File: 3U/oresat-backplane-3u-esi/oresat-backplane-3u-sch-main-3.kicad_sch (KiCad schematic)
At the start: 28 parts

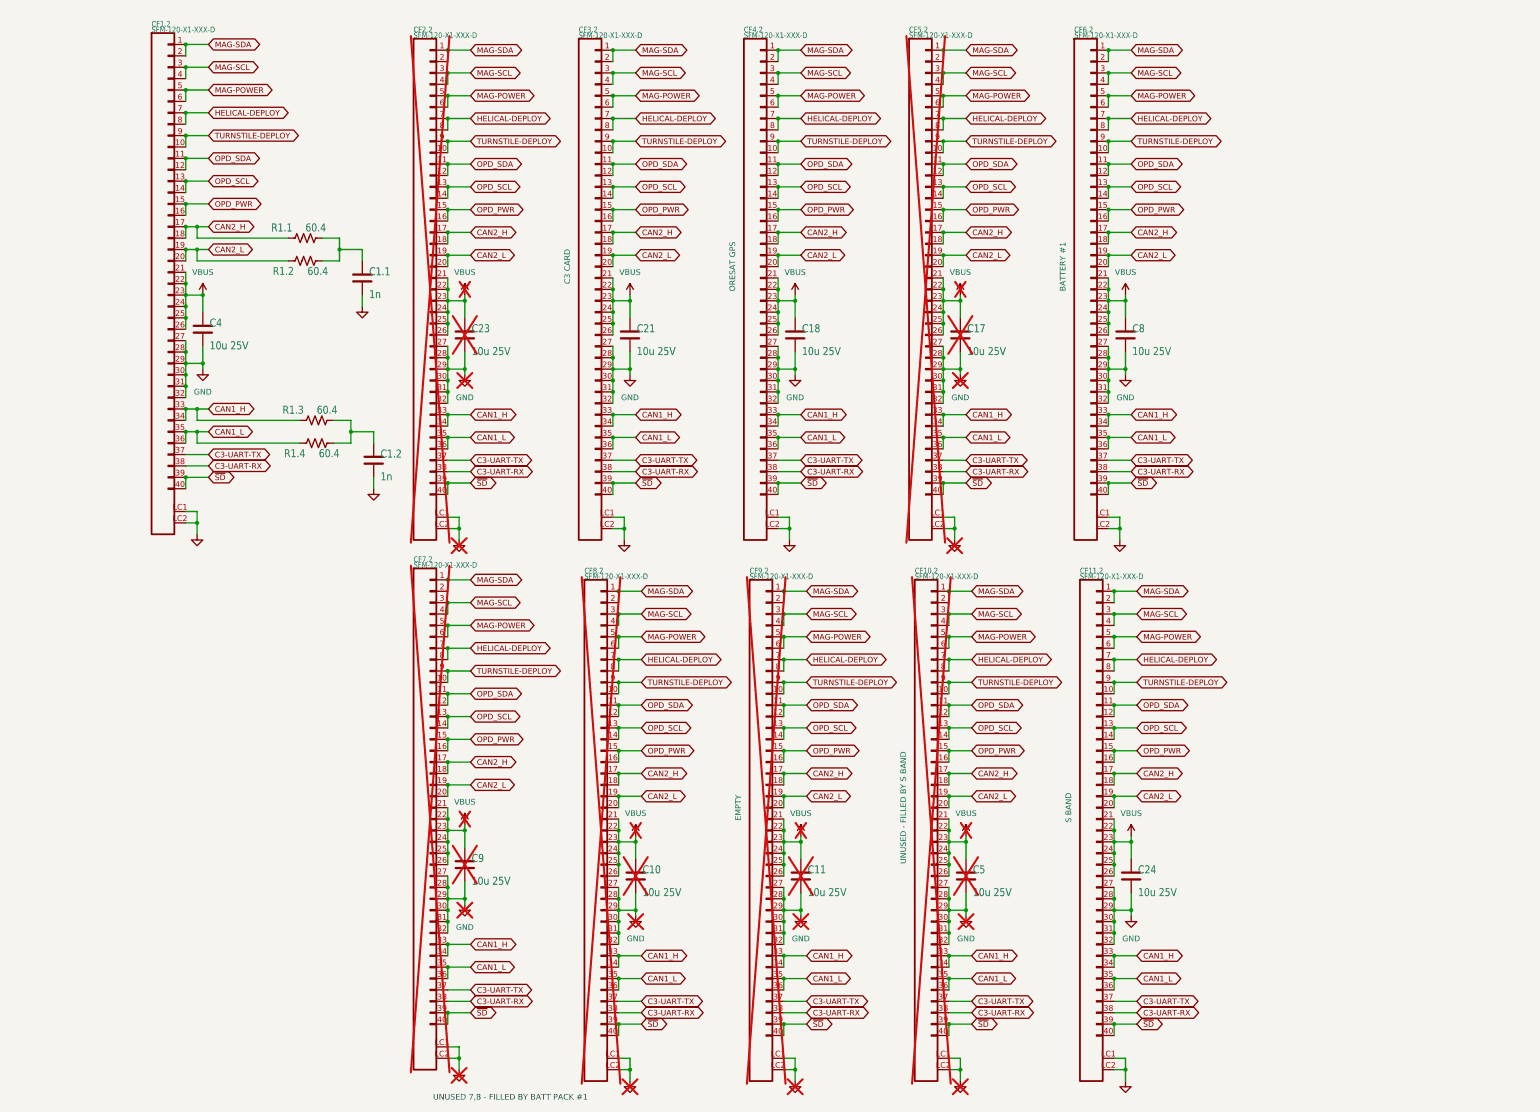
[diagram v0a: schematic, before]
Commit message: Added schematic and board variables, polished some silkscreen, reviewed board, renamed directory
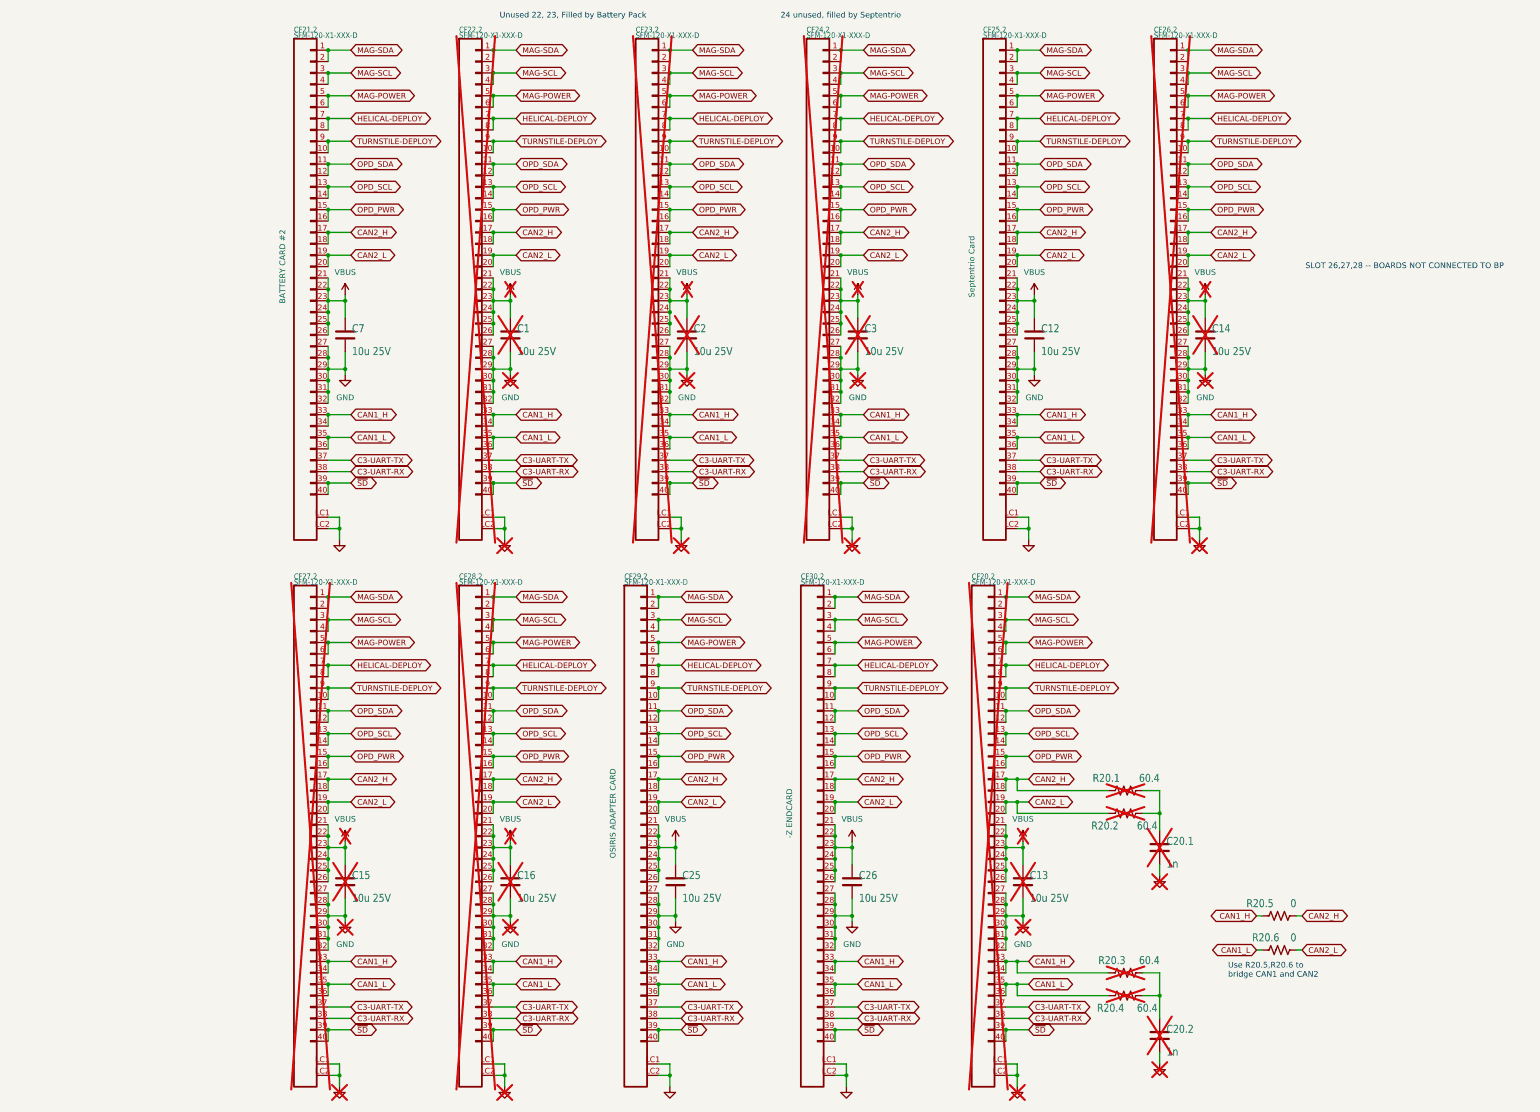
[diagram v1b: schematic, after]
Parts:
- removed C1.1, C1.2: 1n, oresat-passives:0603-C-NOSILK, symbol Device:C
- removed C10, C11, C17, C18, C21, C23, C24, C4, C5, C8, C9: 10u 25V, Capacitor_SMD:C_1206_3216Metric, symbol Device:C
- removed CF1.2, CF10.2, CF11.2, CF2.2, CF3.2, CF4.2, CF5.2, CF6.2, CF7.2, CF8.2, CF9.2: SFM-120-X1-XXX-D, oresat-connectors:J-SAMTEC-SFM-120-X1-XXX-D, symbol oresat-connectors:J-SAMTEC-SFM-120-X1-XXX-D
- removed R1.1, R1.2, R1.3, R1.4: 60.4, Resistor_SMD:R_1206_3216Metric, symbol Device:R_US
- added C1, C12, C13, C14, C15, C16, C2, C25, C26, C3, C7: 10u 25V, Capacitor_SMD:C_1206_3216Metric, symbol Device:C
- added C20.1, C20.2: 1n, oresat-passives:0603-C-NOSILK, symbol Device:C
- added CF20.2, CF21.2, CF22.2, CF23.2, CF24.2, CF25.2, CF26.2, CF27.2, CF28.2, CF29.2, CF30.2: SFM-120-X1-XXX-D, oresat-connectors:J-SAMTEC-SFM-120-X1-XXX-D, symbol oresat-connectors:J-SAMTEC-SFM-120-X1-XXX-D
- added R20.1, R20.2, R20.3, R20.4: 60.4, Resistor_SMD:R_1206_3216Metric, symbol Device:R_US
- added R20.5, R20.6: 0, oresat-passives:0603-C-NOSILK, symbol Device:R_US
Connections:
- net C3-UART-RX: now also CF20.2.38, CF21.2.38, CF22.2.38, CF23.2.38, CF24.2.38, CF25.2.38, CF26.2.38, CF27.2.38, CF28.2.38, CF29.2.38, CF30.2.38
- net C3-UART-TX: now also CF20.2.37, CF21.2.37, CF22.2.37, CF23.2.37, CF24.2.37, CF25.2.37, CF26.2.37, CF27.2.37, CF28.2.37, CF29.2.37, CF30.2.37
- net CAN1_H: now also CF20.2.33, CF20.2.34, CF21.2.33, CF21.2.34, CF22.2.33, CF22.2.34, CF23.2.33, CF23.2.34, CF24.2.33, CF24.2.34, CF25.2.33, CF25.2.34, CF26.2.33, CF26.2.34, CF27.2.33, CF27.2.34, CF28.2.33, CF28.2.34, CF29.2.33, CF29.2.34, CF30.2.33, CF30.2.34, R20.3.1, R20.5.1
- net CAN1_L: now also CF20.2.35, CF20.2.36, CF21.2.35, CF21.2.36, CF22.2.35, CF22.2.36, CF23.2.35, CF23.2.36, CF24.2.35, CF24.2.36, CF25.2.35, CF25.2.36, CF26.2.35, CF26.2.36, CF27.2.35, CF27.2.36, CF28.2.35, CF28.2.36, CF29.2.35, CF29.2.36, CF30.2.35, CF30.2.36, R20.4.2, R20.6.1
- net CAN2_H: now also CF20.2.17, CF20.2.18, CF21.2.17, CF21.2.18, CF22.2.17, CF22.2.18, CF23.2.17, CF23.2.18, CF24.2.17, CF24.2.18, CF25.2.17, CF25.2.18, CF26.2.17, CF26.2.18, CF27.2.17, CF27.2.18, CF28.2.17, CF28.2.18, CF29.2.17, CF29.2.18, CF30.2.17, CF30.2.18, R20.1.1, R20.5.2
- net CAN2_L: now also CF20.2.19, CF20.2.20, CF21.2.19, CF21.2.20, CF22.2.19, CF22.2.20, CF23.2.19, CF23.2.20, CF24.2.19, CF24.2.20, CF25.2.19, CF25.2.20, CF26.2.19, CF26.2.20, CF27.2.19, CF27.2.20, CF28.2.19, CF28.2.20, CF29.2.19, CF29.2.20, CF30.2.19, CF30.2.20, R20.2.2, R20.6.2
- net GND: now also C1.2, C12.2, C13.2, C14.2, C15.2, C16.2, C2.2, C20.1.2, C20.2.2, C25.2, C26.2, C3.2, C7.2, CF20.2.27, CF20.2.28, CF20.2.29, CF20.2.30, CF20.2.31, CF20.2.32, CF20.2.LC1, CF20.2.LC2, CF21.2.27, CF21.2.28, CF21.2.29, CF21.2.30, CF21.2.31, CF21.2.32, CF21.2.LC1, CF21.2.LC2, CF22.2.27, CF22.2.28, CF22.2.29, CF22.2.30, CF22.2.31, CF22.2.32, CF22.2.LC1, CF22.2.LC2, CF23.2.27, CF23.2.28, CF23.2.29, CF23.2.30, CF23.2.31, CF23.2.32, CF23.2.LC1, CF23.2.LC2, CF24.2.27, CF24.2.28, CF24.2.29, CF24.2.30, CF24.2.31, CF24.2.32, CF24.2.LC1, CF24.2.LC2, CF25.2.27, CF25.2.28, CF25.2.29, CF25.2.30, CF25.2.31, CF25.2.32, CF25.2.LC1, CF25.2.LC2, CF26.2.27, CF26.2.28, CF26.2.29, CF26.2.30, CF26.2.31, CF26.2.32, CF26.2.LC1, CF26.2.LC2, CF27.2.27, CF27.2.28, CF27.2.29, CF27.2.30, CF27.2.31, CF27.2.32, CF27.2.LC1, CF27.2.LC2, CF28.2.27, CF28.2.28, CF28.2.29, CF28.2.30, CF28.2.31, CF28.2.32, CF28.2.LC1, CF28.2.LC2, CF29.2.27, CF29.2.28, CF29.2.29, CF29.2.30, CF29.2.31, CF29.2.32, CF29.2.LC1, CF29.2.LC2, CF30.2.27, CF30.2.28, CF30.2.29, CF30.2.30, CF30.2.31, CF30.2.32, CF30.2.LC1, CF30.2.LC2
- net HELICAL-DEPLOY: now also CF20.2.7, CF20.2.8, CF21.2.7, CF21.2.8, CF22.2.7, CF22.2.8, CF23.2.7, CF23.2.8, CF24.2.7, CF24.2.8, CF25.2.7, CF25.2.8, CF26.2.7, CF26.2.8, CF27.2.7, CF27.2.8, CF28.2.7, CF28.2.8, CF29.2.7, CF29.2.8, CF30.2.7, CF30.2.8
- net MAG-POWER: now also CF20.2.5, CF20.2.6, CF21.2.5, CF21.2.6, CF22.2.5, CF22.2.6, CF23.2.5, CF23.2.6, CF24.2.5, CF24.2.6, CF25.2.5, CF25.2.6, CF26.2.5, CF26.2.6, CF27.2.5, CF27.2.6, CF28.2.5, CF28.2.6, CF29.2.5, CF29.2.6, CF30.2.5, CF30.2.6
- net MAG-SCL: now also CF20.2.3, CF20.2.4, CF21.2.3, CF21.2.4, CF22.2.3, CF22.2.4, CF23.2.3, CF23.2.4, CF24.2.3, CF24.2.4, CF25.2.3, CF25.2.4, CF26.2.3, CF26.2.4, CF27.2.3, CF27.2.4, CF28.2.3, CF28.2.4, CF29.2.3, CF29.2.4, CF30.2.3, CF30.2.4
- net MAG-SDA: now also CF20.2.1, CF20.2.2, CF21.2.1, CF21.2.2, CF22.2.1, CF22.2.2, CF23.2.1, CF23.2.2, CF24.2.1, CF24.2.2, CF25.2.1, CF25.2.2, CF26.2.1, CF26.2.2, CF27.2.1, CF27.2.2, CF28.2.1, CF28.2.2, CF29.2.1, CF29.2.2, CF30.2.1, CF30.2.2
- net OPD_PWR: now also CF20.2.15, CF20.2.16, CF21.2.15, CF21.2.16, CF22.2.15, CF22.2.16, CF23.2.15, CF23.2.16, CF24.2.15, CF24.2.16, CF25.2.15, CF25.2.16, CF26.2.15, CF26.2.16, CF27.2.15, CF27.2.16, CF28.2.15, CF28.2.16, CF29.2.15, CF29.2.16, CF30.2.15, CF30.2.16
- net OPD_SCL: now also CF20.2.13, CF20.2.14, CF21.2.13, CF21.2.14, CF22.2.13, CF22.2.14, CF23.2.13, CF23.2.14, CF24.2.13, CF24.2.14, CF25.2.13, CF25.2.14, CF26.2.13, CF26.2.14, CF27.2.13, CF27.2.14, CF28.2.13, CF28.2.14, CF29.2.13, CF29.2.14, CF30.2.13, CF30.2.14
- net OPD_SDA: now also CF20.2.11, CF20.2.12, CF21.2.11, CF21.2.12, CF22.2.11, CF22.2.12, CF23.2.11, CF23.2.12, CF24.2.11, CF24.2.12, CF25.2.11, CF25.2.12, CF26.2.11, CF26.2.12, CF27.2.11, CF27.2.12, CF28.2.11, CF28.2.12, CF29.2.11, CF29.2.12, CF30.2.11, CF30.2.12
- net TURNSTILE-DEPLOY: now also CF20.2.10, CF20.2.9, CF21.2.10, CF21.2.9, CF22.2.10, CF22.2.9, CF23.2.10, CF23.2.9, CF24.2.10, CF24.2.9, CF25.2.10, CF25.2.9, CF26.2.10, CF26.2.9, CF27.2.10, CF27.2.9, CF28.2.10, CF28.2.9, CF29.2.10, CF29.2.9, CF30.2.10, CF30.2.9
- net VBUS: now also C1.1, C12.1, C13.1, C14.1, C15.1, C16.1, C2.1, C25.1, C26.1, C3.1, C7.1, CF20.2.21, CF20.2.22, CF20.2.23, CF20.2.24, CF20.2.25, CF20.2.26, CF21.2.21, CF21.2.22, CF21.2.23, CF21.2.24, CF21.2.25, CF21.2.26, CF22.2.21, CF22.2.22, CF22.2.23, CF22.2.24, CF22.2.25, CF22.2.26, CF23.2.21, CF23.2.22, CF23.2.23, CF23.2.24, CF23.2.25, CF23.2.26, CF24.2.21, CF24.2.22, CF24.2.23, CF24.2.24, CF24.2.25, CF24.2.26, CF25.2.21, CF25.2.22, CF25.2.23, CF25.2.24, CF25.2.25, CF25.2.26, CF26.2.21, CF26.2.22, CF26.2.23, CF26.2.24, CF26.2.25, CF26.2.26, CF27.2.21, CF27.2.22, CF27.2.23, CF27.2.24, CF27.2.25, CF27.2.26, CF28.2.21, CF28.2.22, CF28.2.23, CF28.2.24, CF28.2.25, CF28.2.26, CF29.2.21, CF29.2.22, CF29.2.23, CF29.2.24, CF29.2.25, CF29.2.26, CF30.2.21, CF30.2.22, CF30.2.23, CF30.2.24, CF30.2.25, CF30.2.26
- net ~{SD}: now also CF20.2.39, CF20.2.40, CF21.2.39, CF21.2.40, CF22.2.39, CF22.2.40, CF23.2.39, CF23.2.40, CF24.2.39, CF24.2.40, CF25.2.39, CF25.2.40, CF26.2.39, CF26.2.40, CF27.2.39, CF27.2.40, CF28.2.39, CF28.2.40, CF29.2.39, CF29.2.40, CF30.2.39, CF30.2.40
- new net: C20.2.1, R20.3.2, R20.4.1
- new net: C20.1.1, R20.1.2, R20.2.1
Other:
- note added: "24 unused, filled by Septentrio"
- note added: "SLOT 26,27,28 -- BOARDS NOT CONNECTED TO BP"
- note added: "Unused 22, 23, Filled by Battery Pack"
- note added: "Use R20.5,R20.6 to bridge CAN1 and CAN2"
- note removed: "UNUSED 7,8 - FILLED BY BATT PACK #1"
- company: Portland State Aerospace Society -> PSAS / ESI
- title: Generic OreSat 3U Backplane -> OreSat 3U Backplane for ESI

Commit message: Labelled connectors & disconnected C3 LBand
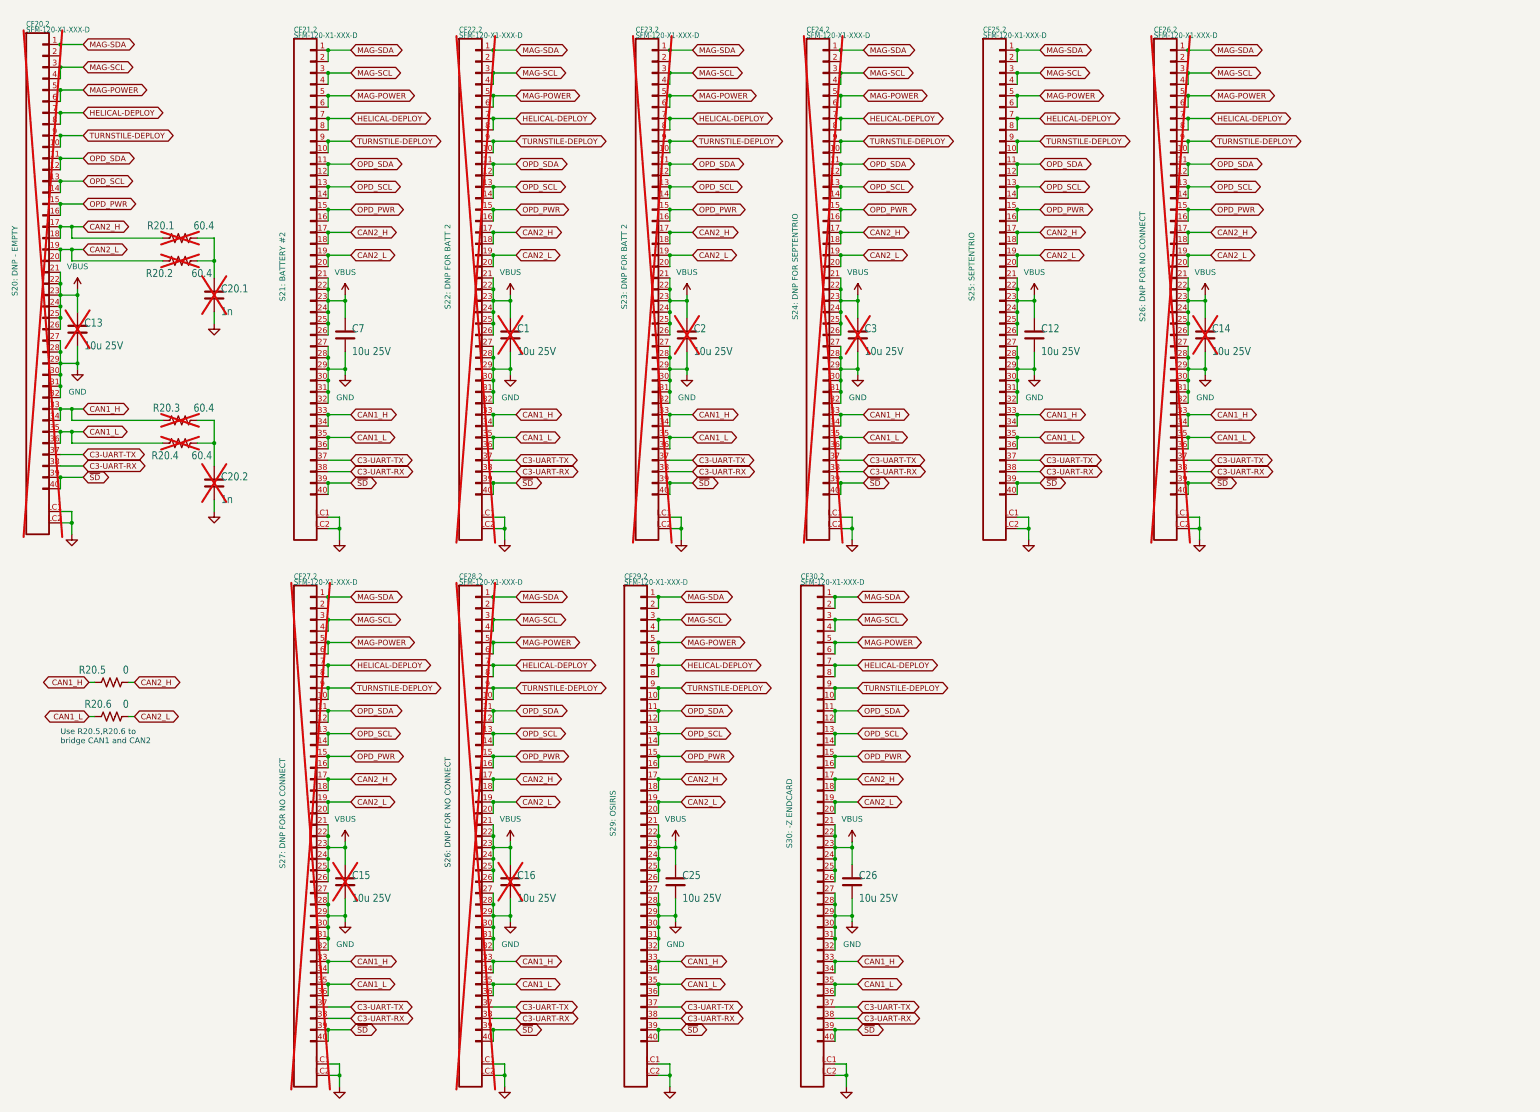
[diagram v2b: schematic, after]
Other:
- note added: "S26: DNP FOR NO CONNECT"
- note removed: "24 unused, filled by Septentrio"
- note removed: "SLOT 26,27,28 -- BOARDS NOT CONNECTED TO BP"
- note removed: "Unused 22, 23, Filled by Battery Pack"
- moved on the sheet: C13, C20.1, C20.2, CF20.2, R20.1, R20.2, R20.3, R20.4, R20.5, R20.6

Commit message: Polish of 3U for ESI
Fixed ERC/DRC/sync errors. Made fancy RF table. Fixed BOM.
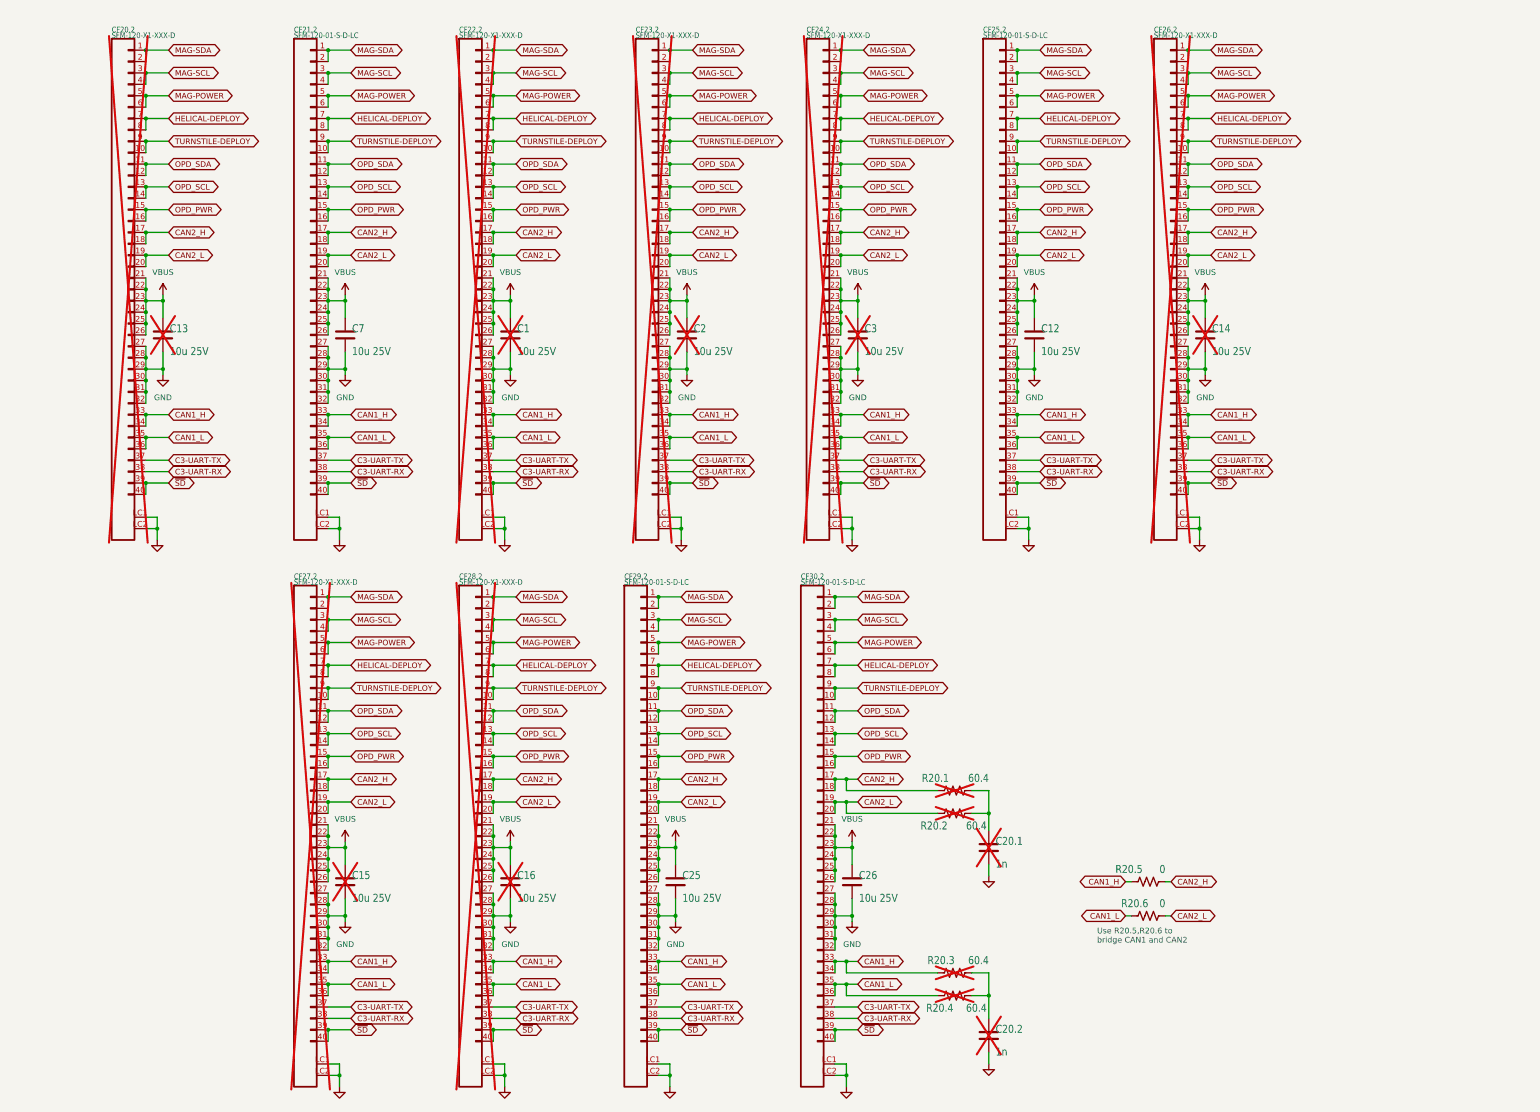
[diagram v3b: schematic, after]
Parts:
- C1, C12, C13, C14, C15, C16, C2, C25, C26, C3, C7: DIS (none) -> DigiKey; DPN (none) -> 587-3485-1-ND; MFR (none) -> Taiyo Yuden; MPN (none) -> TMK316AB7106KLHT
- C20.1, C20.2: DIS (none) -> DigiKey; DPN (none) -> 399-C0603C102J5GECAUTOCT-ND; MFR (none) -> KEMET; MPN (none) -> C0603C102J5GECAUTO
- CF20.2, CF22.2, CF23.2, CF24.2, CF26.2, CF27.2, CF28.2: DIS (none) -> DigiKey; DPN (none) -> SAM11706-ND; MFR (none) -> Samtec Inc.; MPN (none) -> SFM-120-01-S-D-LC
- CF21.2, CF25.2, CF29.2, CF30.2: value SFM-120-X1-XXX-D -> SFM-120-01-S-D-LC; DIS (none) -> DigiKey; DPN (none) -> SAM11706-ND; MFR (none) -> Samtec Inc.; MPN (none) -> SFM-120-01-S-D-LC
- R20.1, R20.2, R20.3, R20.4: DIS (none) -> DigiKey; DPN (none) -> RMCF1206FT60R4CT-ND; MFR (none) -> Stackpole Electronics Inc; MPN (none) -> RMCF1206FT60R4
- R20.5, R20.6: DIS (none) -> DigiKey; DPN (none) -> RMCF0603ZT0R00CT-ND; MFR (none) -> Stackpole Electronics Inc; MPN (none) -> RMCF0603ZT0R00
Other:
- note removed: "S26: DNP FOR NO CONNECT"
- moved on the sheet: C13, C20.1, C20.2, CF20.2, R20.1, R20.2, R20.3, R20.4, R20.5, R20.6
